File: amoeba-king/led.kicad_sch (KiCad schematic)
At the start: 1 part

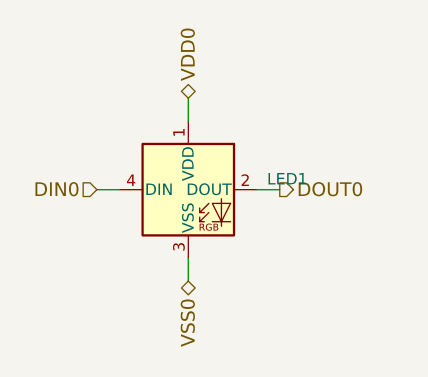
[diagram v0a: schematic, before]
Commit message: Added row via to be used as an anchor point for cabling.
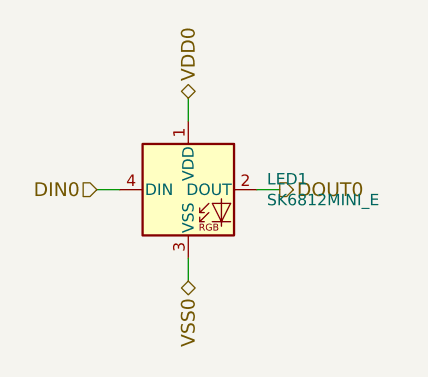
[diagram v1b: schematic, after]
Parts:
- LED1: value (none) -> SK6812MINI_E; footprint (none) -> amoeba-modules:LED_SK6812MINI_E_PLCC4_3.2x2.8mm_Shine_Through
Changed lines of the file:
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@@
       (effects (font (size 1.27 1.27)) (justify left))
     )
-    (property "Value" "" (id 1) (at 150.9776 93.853 0)
+    (property "Value" "SK6812MINI_E" (id 1) (at 150.9776 93.853 0)
       (effects (font (size 1.27 1.27)) (justify left))
     )
-    (property "Footprint" "" (id 2) (at 143.51 100.33 0)
+    (property "Footprint" "amoeba-modules:LED_SK6812MINI_E_PLCC4_3.2x2.8mm_Shine_Through" (id 2) (at 143.51 100.33 0)
       (effects (font (size 1.27 1.27)) (justify left top) hide)
     )
